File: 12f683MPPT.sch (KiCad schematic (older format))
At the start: 47 parts, among them J1 Conn_01x01_Male, J2 Conn_01x01_Male, J3 Conn_01x01_Male, J4 Conn_01x01_Male, Q1 BUK9511-55A127, Q2 BUK9511-55A127, Q3 2N2222A, Q4 2N2222A, Q5 2N2907A, SW1 SW_Push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

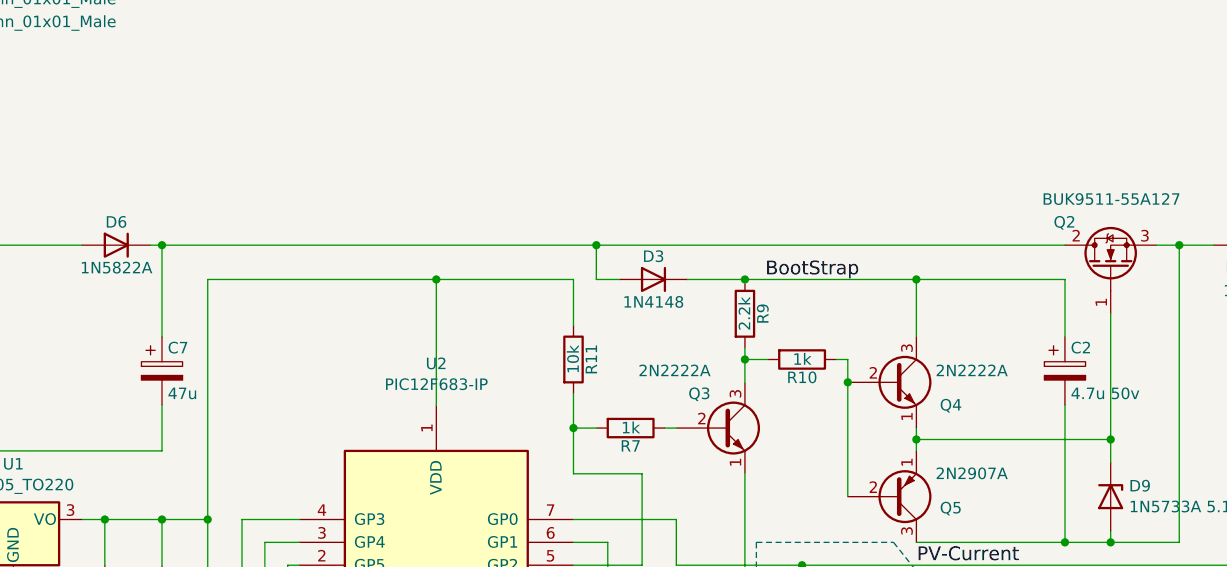
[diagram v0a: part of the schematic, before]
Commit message: Revert and change Diode.
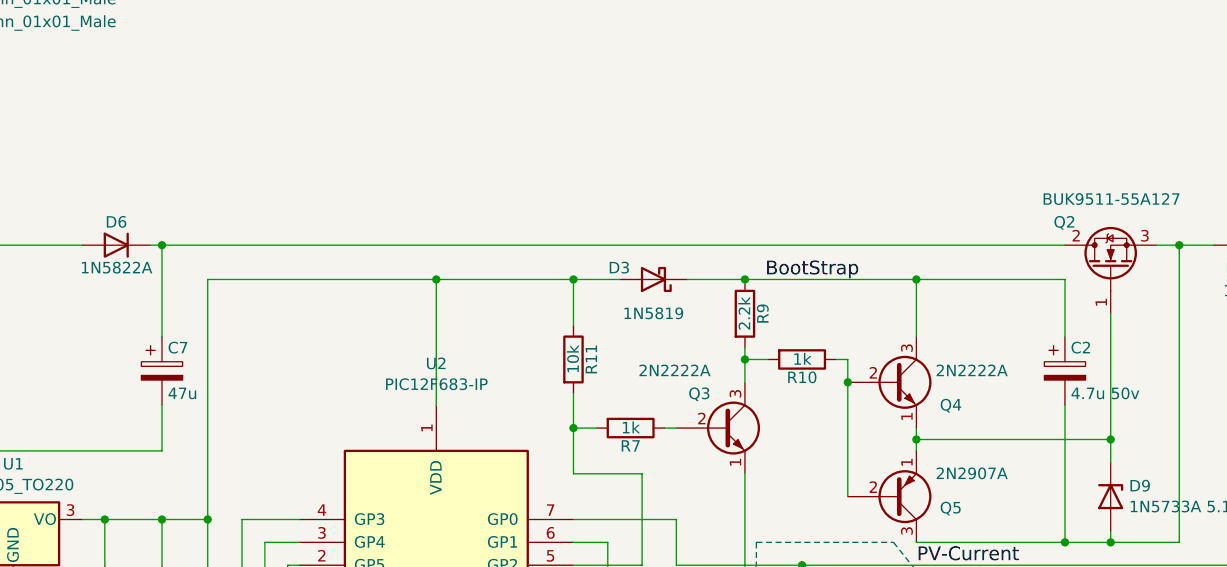
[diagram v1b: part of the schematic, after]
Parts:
- removed D3: 1N4148, Diodes_THT:D_DO-41_SOD81_P10.16mm_Horizontal, symbol Device:D
- added D3: 1N5819, Diode_THT:D_DO-41_SOD81_P10.16mm_Horizontal, symbol Device:D_Schottky
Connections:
- net BootStrap: now also D3.1 (K)
- net at C3.1, C4.1, R11.1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: now also D3.2 (A)
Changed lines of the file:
@@
 Title "Simple MPPT with 12F683"
 Date "2021-07-30"
-Rev "1.2"
+Rev "1.21"
 Comp ""
 Comment1 ""
@@
 $EndComp
 $Comp
-L Device:D D3
-U 1 1 55C36E30
-P 5450 2350
-F 0 "D3" H 5450 2450 50  0000 C CNN
-F 1 "1N4148" H 5450 2250 50  0000 C CNN
-F 2 "Diodes_THT:D_DO-41_SOD81_P10.16mm_Horizontal" H 5450 2350 60  0001 C CNN
-F 3 "" H 5450 2350 60  0000 C CNN
-	1    5450 2350
-	-1   0    0    -1
-$EndComp
-$Comp
 L Device:R R10
 U 1 1 55C376F8
@@
 Connection ~ 8400 5600
 Wire Wire Line
-	3300 2200 5200 2200
-Wire Wire Line
 	2250 2850 2250 3400
 Wire Wire Line
@@
 Connection ~ 7450 3050
 Wire Wire Line
-	5300 2350 5200 2350
-Wire Wire Line
-	5200 2350 5200 2200
-Connection ~ 5200 2200
-Wire Wire Line
-	5200 2200 7250 2200
+	3300 2200 7250 2200
+Wire Wire Line
+	5100 2350 5300 2350
+Connection ~ 5100 2350
+$Comp
+L Device:D_Schottky D3
+U 1 1 6104DF4D
+P 5450 2350
+F 0 "D3" H 5600 2300 50  0000 C CNN
+F 1 "1N5819" H 5450 2500 50  0000 C CNN
+F 2 "Diode_THT:D_DO-41_SOD81_P10.16mm_Horizontal" H 5450 2350 50  0001 C CNN
+F 3 "~" H 5450 2350 50  0001 C CNN
+	1    5450 2350
+	-1   0    0    1
+$EndComp
 $EndSCHEMATC
